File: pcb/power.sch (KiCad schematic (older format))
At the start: 8 parts, among them P2 UNFUSED_PWR, P3 BATT, P5 BATT, U2 MCP1700T-3302E/TT

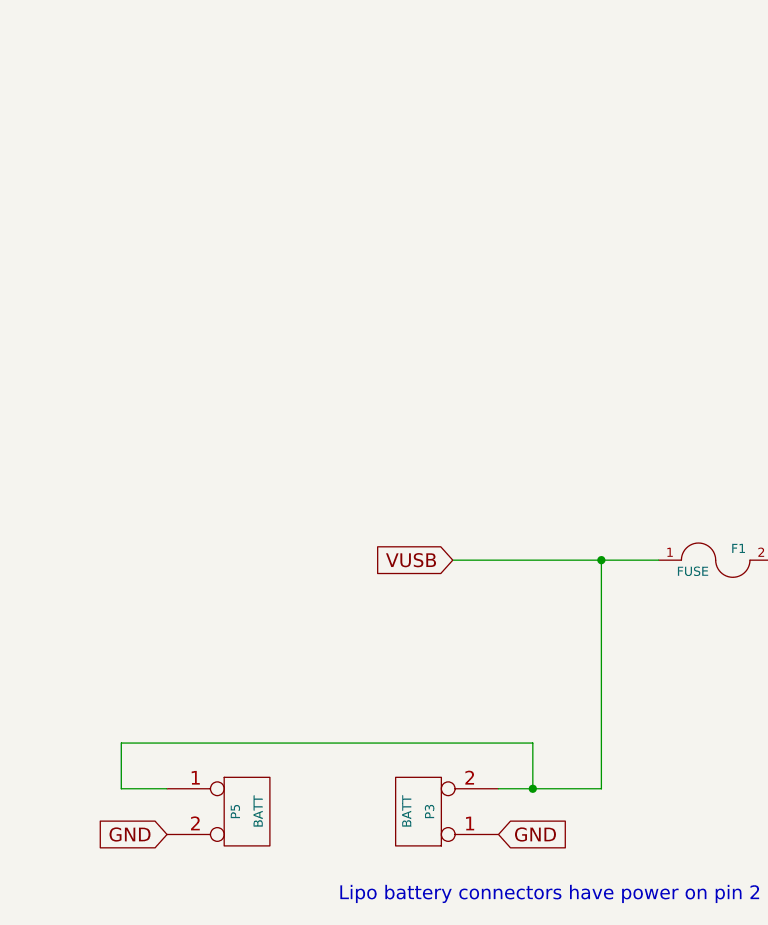
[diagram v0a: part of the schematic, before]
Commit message: Add power choice slide switch to the schematic.
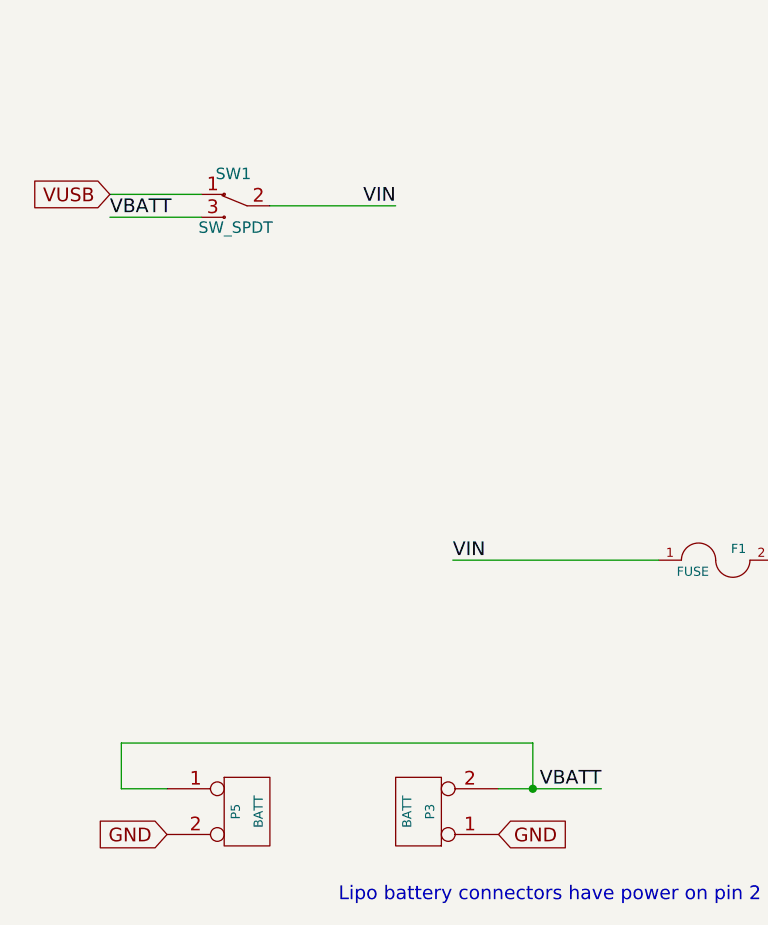
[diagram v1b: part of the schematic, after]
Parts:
- added SW1: SW_SPDT, symbol SW_SPDT
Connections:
- net VUSB: now also SW1.1 (NC); no longer F1.1, P3.2 (PM), P5.1 (P1)
- new net VBATT: P3.2 (PM), P5.1 (P1), SW1.3 (NO)
- new net VIN: F1.1, SW1.2 (COM)
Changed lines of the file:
@@
 	1    0    0    -1
 $EndComp
-Text GLabel 2750 4500 0    60   Input ~ 0
+Text GLabel 1250 2900 0    60   Input ~ 0
 VUSB
 $Comp
@@
 Wire Wire Line
 	2950 5500 3400 5500
+$Comp
+L SW_SPDT SW1
+U 1 1 54B0B8AC
+P 1800 2950
+F 0 "SW1" H 1810 3090 50  0000 C CNN
+F 1 "SW_SPDT" H 1800 2855 50  0000 C CNN
+F 2 "" H 1800 2950 60  0000 C CNN
+F 3 "" H 1800 2950 60  0000 C CNN
+	1    1800 2950
+	-1   0    0    -1
+$EndComp
 Wire Wire Line
-	3400 5500 3400 4500
-Connection ~ 3400 4500
+	1950 2950 2500 2950
+Text Label 2500 2950 2    60   ~ 0
+VIN
+Wire Wire Line
+	1650 2900 1250 2900
+Wire Wire Line
+	1650 3000 1250 3000
+Text Label 2750 4500 0    60   ~ 0
+VIN
+Text Label 3400 5500 2    60   ~ 0
+VBATT
+Text Label 1250 3000 0    60   ~ 0
+VBATT
 $EndSCHEMATC

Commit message: pcb work from last night
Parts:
- removed P2: UNFUSED_PWR, symbol CONN_2
- removed P5: BATT, symbol CONN_2
- added P5: gnd, Pin_Headers:Pin_Header_Straight_1x01, symbol CONN_01X01
- C3, C5: value 22u -> 10u; footprint myelin:SM1206_nosilkscreen -> myelin:SM0805_NOSILKSCREEN
- F1: footprint ~ -> SMD_Packages:SMD-1812
- P3: footprint (none) -> myelin:S2B-PH-SM4-TB(LF)(SN)
- SW1: footprint (none) -> myelin:PIN_ARRAY_3X1
- U2: value MCP1700T-3302E/TT -> MCP1700T; footprint SMD_Packages:SOT-23 -> Housings_SOT-89:SOT89-3_Housing
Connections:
- net GND: now also P5.1 (P1)
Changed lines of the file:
@@
 F 0 "P3" V 2550 5600 40  0000 C CNN
 F 1 "BATT" V 2650 5600 40  0000 C CNN
-F 2 "" H 2600 5600 60  0000 C CNN
+F 2 "myelin:S2B-PH-SM4-TB(LF)(SN)" H 2600 5600 60  0001 C CNN
 F 3 "" H 2600 5600 60  0000 C CNN
 	1    2600 5600
 	-1   0    0    1
-$EndComp
-$Comp
-L CONN_2 P2
-U 1 1 549D503A
-P 5350 4600
-F 0 "P2" V 5300 4600 40  0000 C CNN
-F 1 "UNFUSED_PWR" V 5400 4600 40  0000 C CNN
-F 2 "" H 5350 4600 60  0000 C CNN
-F 3 "" H 5350 4600 60  0000 C CNN
-	1    5350 4600
-	1    0    0    -1
 $EndComp
 Text GLabel 1250 2900 0    60   Input ~ 0
@@
 F 0 "F1" H 4000 4550 40  0000 C CNN
 F 1 "FUSE" H 3800 4450 40  0000 C CNN
-F 2 "~" H 3900 4500 60  0000 C CNN
+F 2 "SMD_Packages:SMD-1812" H 3900 4650 60  0000 C CNN
 F 3 "~" H 3900 4500 60  0000 C CNN
 	1    3900 4500
@@
 $EndComp
 Text GLabel 2950 5700 2    60   Input ~ 0
-GND
-Text GLabel 5000 4700 0    60   Input ~ 0
 GND
 $Comp
@@
 P 7400 4550
 F 0 "C5" H 7400 4650 40  0000 L CNN
-F 1 "22u" H 7406 4465 40  0000 L CNN
-F 2 "myelin:SM1206_nosilkscreen" V 7550 4550 30  0000 C CNN
+F 1 "10u" H 7406 4465 40  0000 L CNN
+F 2 "myelin:SM0805_NOSILKSCREEN" V 7550 4550 30  0000 C CNN
 F 3 "~" H 7400 4550 60  0000 C CNN
 	1    7400 4550
@@
 P 6250 4550
 F 0 "C3" H 6250 4650 40  0000 L CNN
-F 1 "22u" H 6256 4465 40  0000 L CNN
-F 2 "myelin:SM1206_nosilkscreen" V 6150 4550 30  0000 C CNN
+F 1 "10u" H 6256 4465 40  0000 L CNN
+F 2 "myelin:SM0805_NOSILKSCREEN" V 6150 4550 30  0001 C CNN
 F 3 "~" H 6250 4550 60  0000 C CNN
 	1    6250 4550
@@
 Wire Wire Line
 	2750 4500 3650 4500
-Wire Wire Line
-	4150 4500 5000 4500
-Connection ~ 4600 4500
 Wire Wire Line
 	6950 4600 6950 4850
@@
 Wire Wire Line
 	7350 4300 7950 4300
-$Comp
-L CONN_2 P5
-U 1 1 549E81C9
-P 1850 5600
-F 0 "P5" V 1800 5600 40  0000 C CNN
-F 1 "BATT" V 1900 5600 40  0000 C CNN
-F 2 "" H 1850 5600 60  0000 C CNN
-F 3 "" H 1850 5600 60  0000 C CNN
-	1    1850 5600
-	1    0    0    -1
-$EndComp
-Wire Wire Line
-	1500 5500 1300 5500
-Wire Wire Line
-	1300 5500 1300 5300
-Wire Wire Line
-	1300 5300 3100 5300
-Wire Wire Line
-	3100 5300 3100 5500
-Connection ~ 3100 5500
-Text GLabel 1500 5700 0    60   Input ~ 0
-GND
 Wire Wire Line
 	4600 4300 4600 4500
@@
 P 6950 4350
 F 0 "U2" H 7100 4154 60  0000 C CNN
-F 1 "MCP1700T-3302E/TT" H 6950 4550 60  0000 C CNN
-F 2 "SMD_Packages:SOT-23" H 6950 4650 60  0000 C CNN
+F 1 "MCP1700T" H 6950 4550 60  0000 C CNN
+F 2 "Housings_SOT-89:SOT89-3_Housing" H 6950 4650 60  0000 C CNN
 F 3 "" H 6950 4350 60  0000 C CNN
 	1    6950 4350
@@
 F 0 "SW1" H 1810 3090 50  0000 C CNN
 F 1 "SW_SPDT" H 1800 2855 50  0000 C CNN
-F 2 "" H 1800 2950 60  0000 C CNN
+F 2 "myelin:PIN_ARRAY_3X1" H 1800 2950 60  0001 C CNN
 F 3 "" H 1800 2950 60  0000 C CNN
 	1    1800 2950
@@
 Text Label 1250 3000 0    60   ~ 0
 VBATT
+Wire Wire Line
+	4600 4500 4150 4500
+$Comp
+L CONN_01X01 P5
+U 1 1 54B46D85
+P 1850 5000
+F 0 "P5" H 1850 5100 50  0000 C CNN
+F 1 "gnd" V 1950 5000 50  0000 C CNN
+F 2 "Pin_Headers:Pin_Header_Straight_1x01" H 1850 5000 60  0001 C CNN
+F 3 "" H 1850 5000 60  0000 C CNN
+	1    1850 5000
+	1    0    0    -1
+$EndComp
+Text GLabel 1650 5000 0    60   Input ~ 0
+GND
 $EndSCHEMATC
